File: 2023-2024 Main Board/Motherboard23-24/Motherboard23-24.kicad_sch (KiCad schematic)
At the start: 0 parts

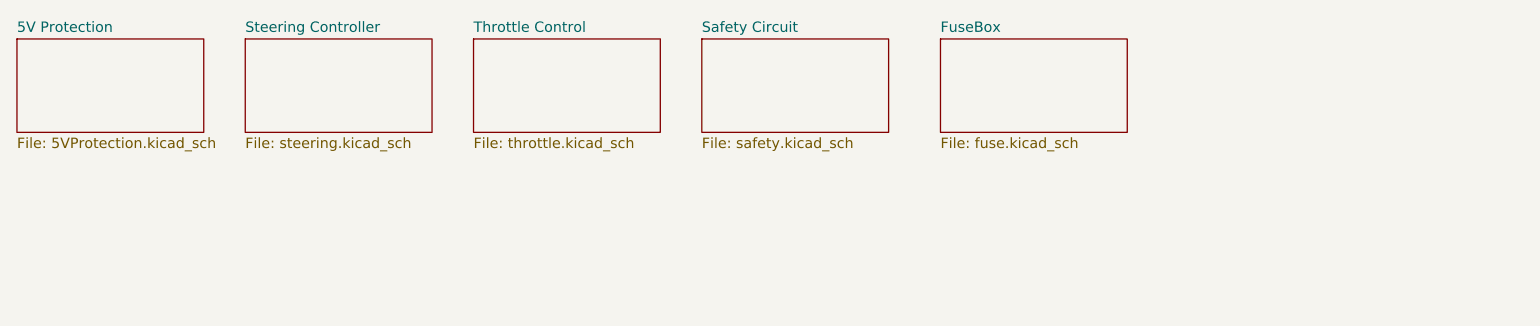
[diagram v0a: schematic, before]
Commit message: Added Schematic for Steering and Throttle
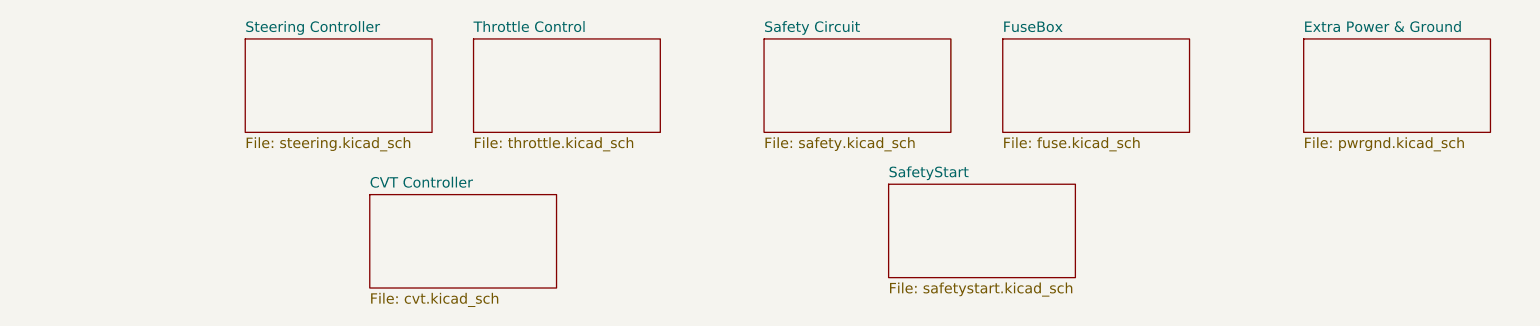
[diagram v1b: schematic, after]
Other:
- removed sheet 5V Protection
- added sheet CVT Controller (cvt.kicad_sch)
- added sheet Extra Power & Ground (pwrgnd.kicad_sch)
- added sheet SafetyStart (safetystart.kicad_sch)
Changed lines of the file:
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@@
     )
   )
-  (sheet (at 123.19 62.23) (size 22.86 11.43) (fields_autoplaced)
+  (sheet (at 130.81 62.23) (size 22.86 11.43) (fields_autoplaced)
     (stroke (width 0.1524) (type solid))
     (fill (color 255 54 79 0.5000))
-    (property "Sheetname" "Safety Circuit" (at 123.19 61.5184 0)
+    (property "Sheetname" "Safety Circuit" (at 130.81 61.5184 0)
       (effects (font (size 1.27 1.27)) (justify left bottom))
     )
-    (property "Sheetfile" "safety.kicad_sch" (at 123.19 74.2446 0)
+    (property "Sheetfile" "safety.kicad_sch" (at 130.81 74.2446 0)
       (effects (font (size 1.27 1.27)) (justify left top))
     )
@@
     )
   )
-  (sheet (at 152.4 62.23) (size 22.86 11.43) (fields_autoplaced)
+  (sheet (at 146.05 80.01) (size 22.86 11.43) (fields_autoplaced)
     (stroke (width 0.1524) (type solid))
     (fill (color 255 54 79 0.5000))
-    (property "Sheetname" "FuseBox" (at 152.4 61.5184 0)
+    (property "Sheetname" "SafetyStart" (at 146.05 79.2984 0)
       (effects (font (size 1.27 1.27)) (justify left bottom))
     )
-    (property "Sheetfile" "fuse.kicad_sch" (at 152.4 74.2446 0)
+    (property "Sheetfile" "safetystart.kicad_sch" (at 146.05 92.0246 0)
+      (effects (font (size 1.27 1.27)) (justify left top))
+    )
+    (instances
+      (project "Motherboard23-24"
+        (path "/418d1727-08ff-41e8-954f-e6e13e4fb4ca" (page "9"))
+      )
+    )
+  )
+  (sheet (at 160.02 62.23) (size 22.86 11.43) (fields_autoplaced)
+    (stroke (width 0.1524) (type solid))
+    (fill (color 255 54 79 0.5000))
+    (property "Sheetname" "FuseBox" (at 160.02 61.5184 0)
+      (effects (font (size 1.27 1.27)) (justify left bottom))
+    )
+    (property "Sheetfile" "fuse.kicad_sch" (at 160.02 74.2446 0)
       (effects (font (size 1.27 1.27)) (justify left top))
     )
@@
     )
   )
-  (sheet (at 39.37 62.23) (size 22.86 11.43) (fields_autoplaced)
+  (sheet (at 196.85 62.23) (size 22.86 11.43) (fields_autoplaced)
     (stroke (width 0.1524) (type solid))
     (fill (color 255 54 79 0.5000))
-    (property "Sheetname" "5V Protection" (at 39.37 61.5184 0)
+    (property "Sheetname" "Extra Power & Ground" (at 196.85 61.5184 0)
       (effects (font (size 1.27 1.27)) (justify left bottom))
     )
-    (property "Sheetfile" "5VProtection.kicad_sch" (at 39.37 74.2446 0)
+    (property "Sheetfile" "pwrgnd.kicad_sch" (at 196.85 74.2446 0)
       (effects (font (size 1.27 1.27)) (justify left top))
+    )
+    (property "Field2" "" (at 196.85 62.23 0)
+      (effects (font (size 1.27 1.27)) hide)
     )
     (instances
       (project "Motherboard23-24"
-        (path "/418d1727-08ff-41e8-954f-e6e13e4fb4ca" (page "4"))
+        (path "/418d1727-08ff-41e8-954f-e6e13e4fb4ca" (page "7"))
       )
     )
@@
       )
     )
+  )
+  (sheet (at 82.55 81.28) (size 22.86 11.43) (fields_autoplaced)
+    (stroke (width 0.1524) (type solid))
+    (fill (color 255 54 79 0.5000))
+    (property "Sheetname" "CVT Controller" (at 82.55 80.5684 0)
+      (effects (font (size 1.27 1.27)) (justify left bottom))
+    )
+    (property "Sheetfile" "cvt.kicad_sch" (at 82.55 93.2946 0)
+      (effects (font (size 1.27 1.27)) (justify left top))
+    )
+    (property "Field2" "" (at 82.55 81.28 0)
+      (effects (font (size 1.27 1.27)) hide)
+    )
+    (instances
+      (project "Motherboard23-24"
+        (path "/418d1727-08ff-41e8-954f-e6e13e4fb4ca" (page "8"))
+      )
+    )
